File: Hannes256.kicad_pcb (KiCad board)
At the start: 2 copper layers, 45.2 x 62.7 mm, 20 parts, among them J1 TED_SOCKET, J2 RAM_SELECTOR, J3 CONN_CS, U1 MOS_7360_TED, U2 74LS257, U3 74LS257, U4 XX4256, U5 XX4256, U6 GAL20V8, U7 74HCT74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

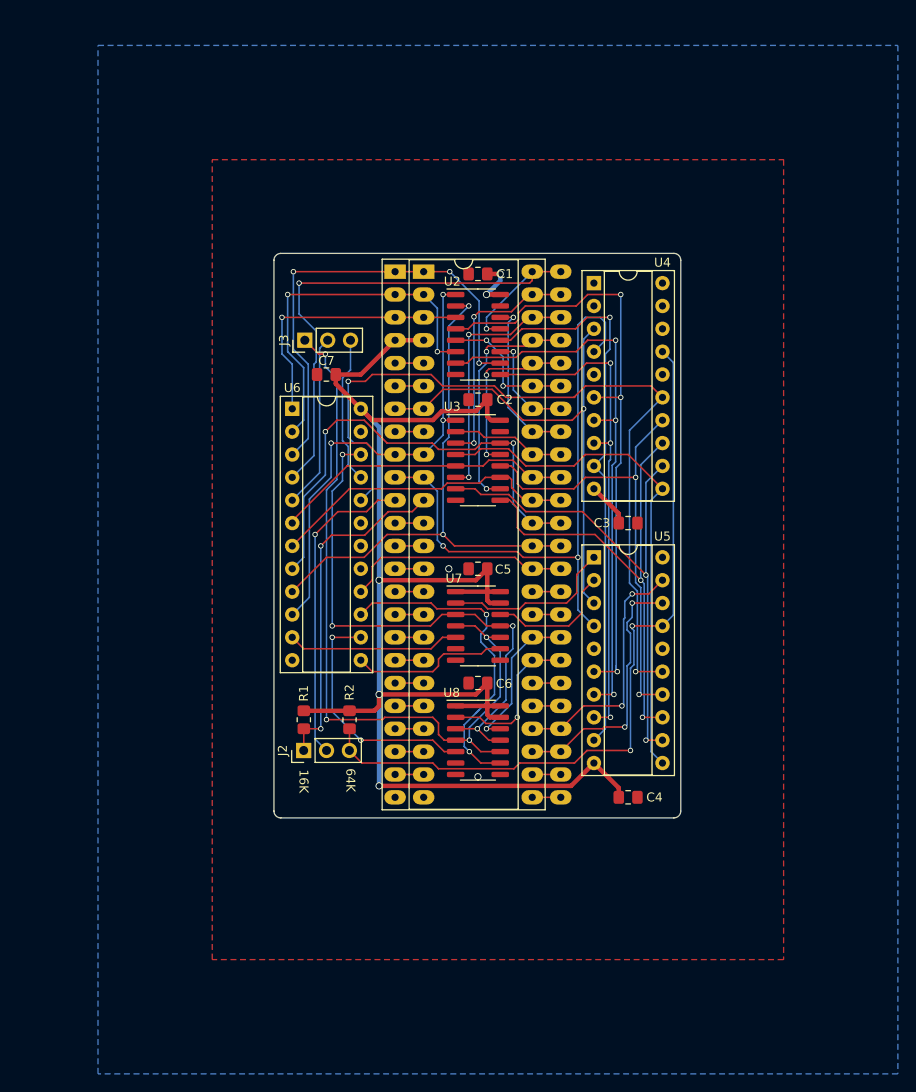
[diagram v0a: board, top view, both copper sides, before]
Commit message: Switch to 41256 RAM This will handle the refresh properly despite needing 8 chips instead of 2, sigh...
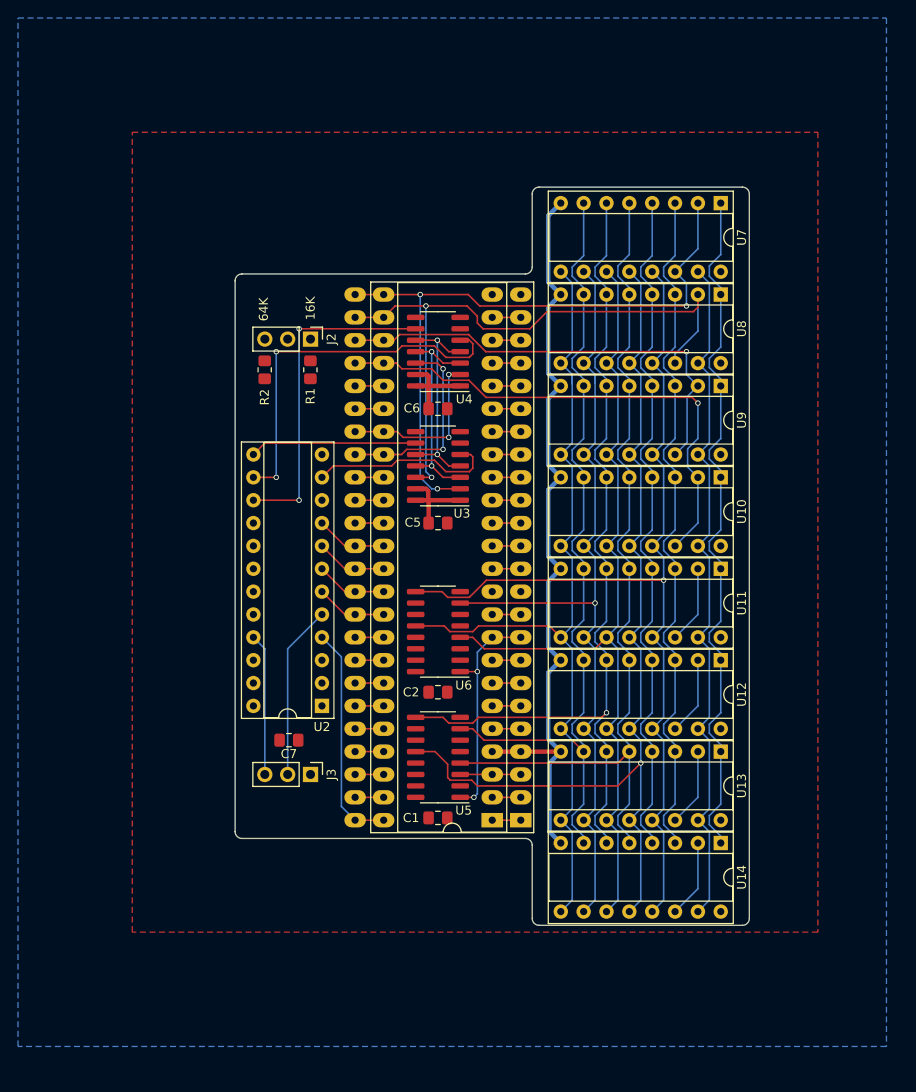
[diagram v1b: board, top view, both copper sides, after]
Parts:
- removed C3, C4: 100n, Capacitor_SMD:C_0805_2012Metric_Pad1.18x1.45mm_HandSolder
- removed the U4 at (144.0, 77.2)
- removed the U5 at (144.0, 107.7)
- added U10: 41256, Package_DIP:DIP-16_W7.62mm_Socket, F.Cu at (158.1, 98.8)
- added U11: 41256, Package_DIP:DIP-16_W7.62mm_Socket, F.Cu at (158.1, 109.0)
- added U12: 41256, Package_DIP:DIP-16_W7.62mm_Socket, F.Cu at (158.1, 119.1)
- added U13: 41256, Package_DIP:DIP-16_W7.62mm_Socket, F.Cu at (158.1, 129.3)
- added U14: 41256, Package_DIP:DIP-16_W7.62mm_Socket, F.Cu at (158.1, 139.4)
- added U7: 41256, Package_DIP:DIP-16_W7.62mm_Socket, F.Cu at (158.1, 68.3)
- added U8: 41256, Package_DIP:DIP-16_W7.62mm_Socket, F.Cu at (158.1, 78.5)
- added U9: 41256, Package_DIP:DIP-16_W7.62mm_Socket, F.Cu at (158.1, 88.6)
- moved U1 62.5 mm to (135.9, 136.9), turned to 180 degrees
- moved J1 61.4 mm to (132.7, 136.9), turned to 180 degrees
- moved C1 60.6 mm to (126.7, 136.7), turned to 0 degrees
- moved J3 48.3 mm to (112.5, 131.8), turned to 270 degrees
- moved U5 47.2 mm to (126.7, 129.9), turned to 180 degrees
- moved J2 45.7 mm to (112.5, 83.4), turned to 270 degrees
- moved U4 43.4 mm to (126.7, 84.8), turned to 180 degrees
- moved C7 40.9 mm to (110.1, 128.0), turned to 0 degrees
- moved R2 40.0 mm to (107.4, 86.9), turned to 90 degrees
- moved R1 38.9 mm to (112.5, 86.9), turned to 90 degrees
- moved U2 33.2 mm to (113.8, 124.2), turned to 180 degrees
- moved C2 32.8 mm to (126.7, 122.7), turned to 0 degrees
- moved C6 30.8 mm to (126.7, 91.2), turned to 0 degrees
- moved U6 19.6 mm to (126.7, 116.0), turned to 180 degrees
- moved U3 18.3 mm to (126.7, 97.5), turned to 180 degrees
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- renumbered U6 to U2, U7 to U3, U8 to U4, U2 to U5, U3 to U6
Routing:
- net +5V: track 173.9 -> 107.3 mm, vias 5 -> 0
- net ~RESET: track 85.4 -> 23.7 mm, vias 4 -> 2
- net d1: track 17.8 -> 72.3 mm, vias 0 -> 2
- net a15: track 61.0 -> 7.91 mm, vias 2 -> 0
- net d0: track 22.6 -> 75.7 mm, vias 0 -> 3
- net m6: track 54.5 -> 107.1 mm, vias 2 -> 1
- net a2: track 53.0 -> 3.17 mm, vias 3 -> 0
- net m3: track 62.0 -> 107.0 mm
- net a14: track 52.7 -> 7.91 mm, vias 2 -> 0
- net m7: track 52.0 -> 96.6 mm, vias 2 -> 0
- net m2: track 56.0 -> 100.4 mm, vias 3 -> 1
- net a3: track 63.6 -> 25.0 mm, vias 2 -> 0
- net /~cas_16k: track 38.2 -> 0.00 mm, vias 2 -> 0
- net m4: track 57.7 -> 95.8 mm
- net /~RAS~/~CAS~ Generation/~cs_ram: track 61.2 -> 23.7 mm, vias 4 -> 2
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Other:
- board size 45.2 x 62.7 mm -> 57.1 x 82 mm

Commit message: Routing almost done
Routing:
- net +5V: track 107.3 -> 228.3 mm, vias 0 -> 3
- net m8: track 78.5 -> 133.6 mm
- net /~cas: track 0.00 -> 53.4 mm, vias 0 -> 1
- net ~RESET: track 23.7 -> 75.1 mm, vias 2 -> 4
- net /~cas_16k: track 0.00 -> 49.2 mm, vias 0 -> 1
- net a2: track 3.17 -> 41.5 mm, vias 0 -> 2
- net /~RAS~/~CAS~ Generation/~cs_ram: track 23.7 -> 61.8 mm, vias 2 -> 4
- net a1: track 3.17 -> 40.9 mm, vias 0 -> 3
- net a15: track 7.91 -> 45.6 mm, vias 0 -> 2
- net MUX: track 25.2 -> 56.1 mm, vias 2 -> 3
- net a4: track 3.18 -> 29.8 mm, vias 0 -> 2
- net a5: track 3.18 -> 29.6 mm, vias 0 -> 2
- net a6: track 3.18 -> 27.1 mm, vias 0 -> 2
- net a0: track 6.73 -> 29.0 mm, vias 0 -> 1
- net m3: track 107.0 -> 128.5 mm, vias 1 -> 2
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
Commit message: Initial routing complete
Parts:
- moved U10 0.51 mm to (158.6, 98.8)
- moved U11 0.51 mm to (158.6, 109.0)
- moved U12 0.51 mm to (158.6, 119.1)
- moved U13 0.51 mm to (158.6, 129.3)
- moved U14 0.51 mm to (158.6, 139.4)
- moved U7 0.51 mm to (158.6, 68.3)
- moved U8 0.51 mm to (158.6, 78.5)
- moved U9 0.51 mm to (158.6, 88.6)
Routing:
- net d5: track 11.8 -> 93.6 mm, vias 0 -> 3
- net d7: track 31.0 -> 104.5 mm, vias 2 -> 4
- net d6: track 27.6 -> 95.6 mm, vias 2 -> 5
- net d4: track 11.8 -> 74.0 mm, vias 0 -> 4
- net ~CAS_64K: track 80.9 -> 140.1 mm, vias 0 -> 1
- net m5: track 100.4 -> 103.0 mm
- net +5V: track 228.3 -> 229.8 mm
- net a1: track 40.9 -> 41.9 mm
- net a9: track 12.8 -> 12.0 mm
- net a3: track 34.6 -> 33.8 mm
- net MUX: track 56.1 -> 56.9 mm
- net a2: track 41.5 -> 42.2 mm, vias 2 -> 3
- net /~RAS~/~CAS~ Generation/~cs_ram: track 61.8 -> 62.4 mm
- net d3: track 57.8 -> 58.4 mm
- net d0: track 74.4 -> 75.0 mm
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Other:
- board text added: "GAL20V8 OR GAL22V16"

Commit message: Yeah yeah yeah
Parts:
- U5, U6: value 74LS257 -> 74HCT257
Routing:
- net d7: track 104.5 -> 100.6 mm
- net d5: track 93.6 -> 96.7 mm
- net /~cas_16k: track 49.2 -> 51.7 mm, vias 2 -> 1
- net /~RAS~/~CAS~ Generation/p6: track 42.0 -> 40.8 mm
- net ~RAS: track 96.8 -> 97.5 mm
- net d4: track 74.0 -> 73.3 mm
- net /~cas: track 53.4 -> 53.9 mm
- net GND: vias 7 -> 8
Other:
- board size 57.1 x 82 mm -> 56.3 x 82 mm
- board text added: "ON C16: - ~CS_OUT~ IS PIN 10 OF U11 - ~CS_IN~ IS *LIFTED* PIN 16 OF U16 - ~RESET~ IS PIN 2 OF U9 OR PIN 40 OF U2 ON +4 IF YOU'RE SMART ENOUGH TO FIT THE BOARD, YOU CAN ALSO FIGURE OUT THE PINS"
- board text added: "V1"
- board text added: "~CS_IN"
- board text added: "~CS_OUT"
- board text added: "~RESET"

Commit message: Add credits
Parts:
- added C10: 100n, Capacitor_SMD:C_0805_2012Metric_Pad1.18x1.45mm_HandSolder, F.Cu at (143.2, 102.6)
- added C11: 100n, Capacitor_SMD:C_0805_2012Metric_Pad1.18x1.45mm_HandSolder, F.Cu at (143.2, 112.8)
- added C12: 100n, Capacitor_SMD:C_0805_2012Metric_Pad1.18x1.45mm_HandSolder, F.Cu at (143.2, 122.7)
- added C13: 100n, Capacitor_SMD:C_0805_2012Metric_Pad1.18x1.45mm_HandSolder, F.Cu at (143.2, 132.0)
- added C14: 100n, Capacitor_SMD:C_0805_2012Metric_Pad1.18x1.45mm_HandSolder, F.Cu at (143.2, 143.1)
- added C7: 100n, Capacitor_SMD:C_0805_2012Metric_Pad1.18x1.45mm_HandSolder, F.Cu at (143.2, 72.1)
- added C8: 100n, Capacitor_SMD:C_0805_2012Metric_Pad1.18x1.45mm_HandSolder, F.Cu at (143.2, 82.3)
- added C9: 100n, Capacitor_SMD:C_0805_2012Metric_Pad1.18x1.45mm_HandSolder, F.Cu at (143.2, 92.5)
- renumbered C7 to C2, C5 to C3, C6 to C4, C1 to C5, C2 to C6
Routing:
- net +5V: track 229.8 -> 256.5 mm, vias 3 -> 7
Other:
- board text added: "256k RAM Expansion for Commodore 16 Based on work by Hannes and Solder/Synergy"
- board text added: "CC-BY-NC-SA © SukkoPera 2022 github.com/ SukkoPera/ Hannes256"

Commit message: Add logo and ready for V1rc1
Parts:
- added V0: CC_LOGO, Hannes256:cc_by_nc_sa, B.Cu at (149.7, 72.1)
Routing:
- net a10: track 20.3 -> 19.5 mm
- net a14: track 19.8 -> 19.0 mm
- net GND: vias 8 -> 10

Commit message: Cosmetic fixes
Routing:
- net MUX: track 56.8 -> 56.1 mm
